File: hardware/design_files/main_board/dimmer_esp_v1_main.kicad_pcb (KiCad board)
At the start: 4 copper layers, 44 x 48.1 mm, 54 parts, among them IC1 PEC11S-929K-S0015, J1 Screw_Terminal_01x03, J2 SM05B-SRSS-TB_LF__SN_, J3 Conn_01x02, K1 FTR-LYCA005Y, Q1 BC817, SW1 Commission, SW2 Toggle, SW3 Reset, U1 SGM2212-3.3XKC3G/TR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

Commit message: Hardware: Switch button pin from GPIO09 (strapping pin) to GPIO23
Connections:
- R9 pad 2: /D09 -> /D23_commission
- SW1 pad 2: /D09 -> /D23_commission
- U4 pad 29: unconnected-(U4-IO23-Pad29) -> /D23_commission
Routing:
- net /D09: track 70.5 -> 0.00 mm, vias 3 -> 0
- net /D23_commission: track 0.00 -> 65.1 mm, vias 0 -> 4
- net GND: track 261.9 -> 263.3 mm
- net /D14: track 39.0 -> 38.4 mm

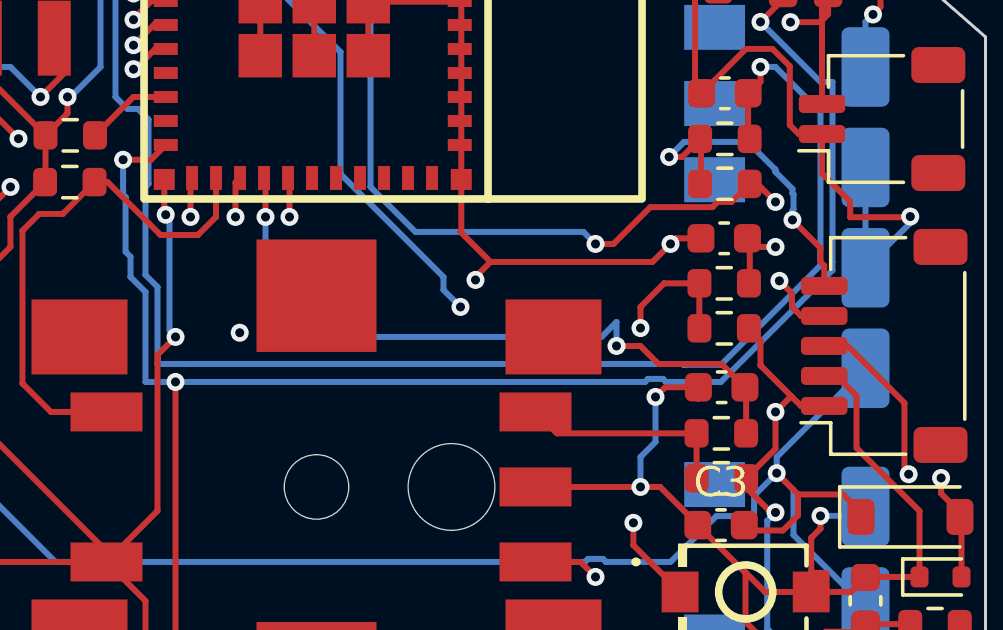
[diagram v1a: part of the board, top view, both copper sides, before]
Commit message: Hardware: Rename C9 back to C8, fix tracks
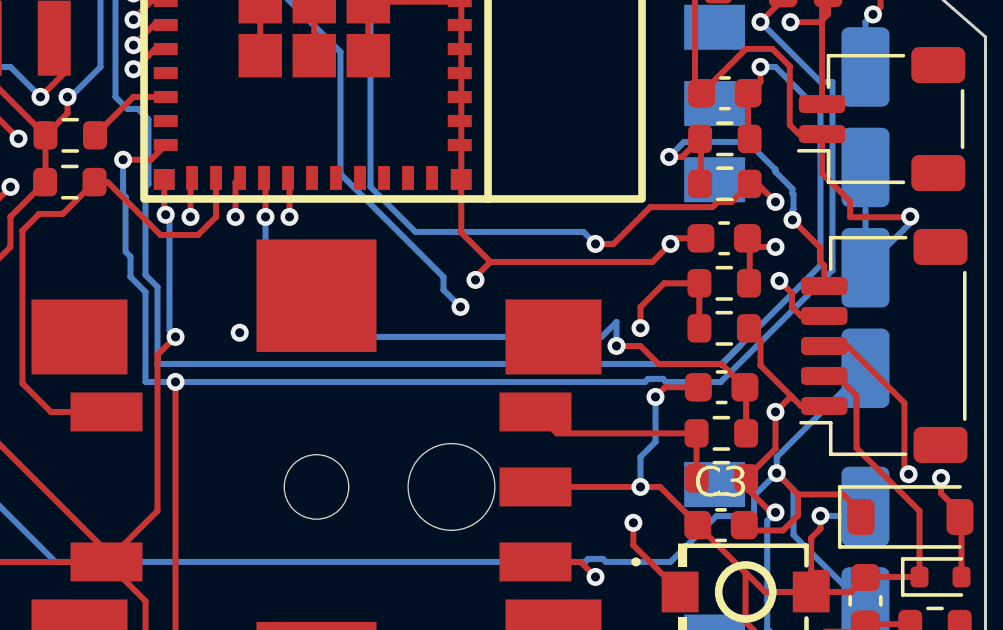
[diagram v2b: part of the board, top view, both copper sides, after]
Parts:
- renumbered C9 to C8
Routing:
- net /D06: track 50.3 -> 51.1 mm

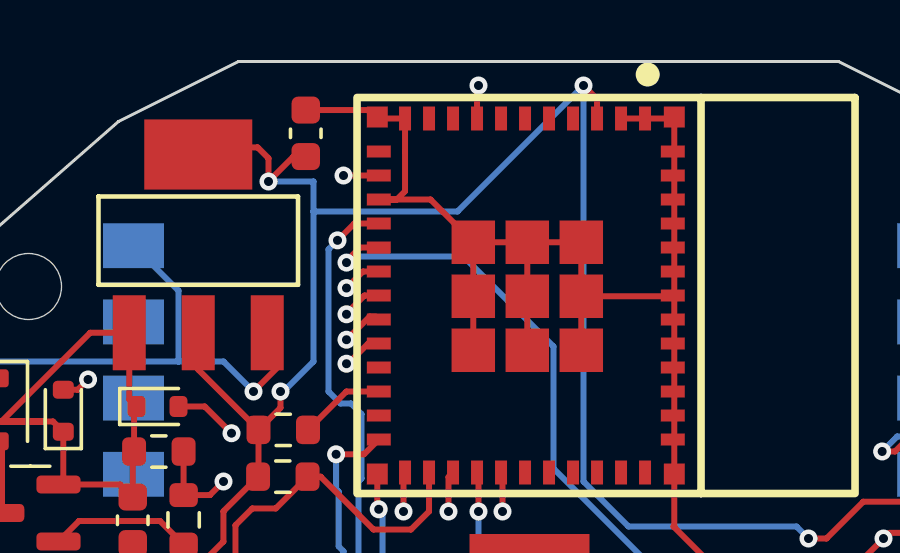
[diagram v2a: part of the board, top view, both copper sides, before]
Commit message: Hardware: Switch relay pin from D15 (strapping pin) to D02
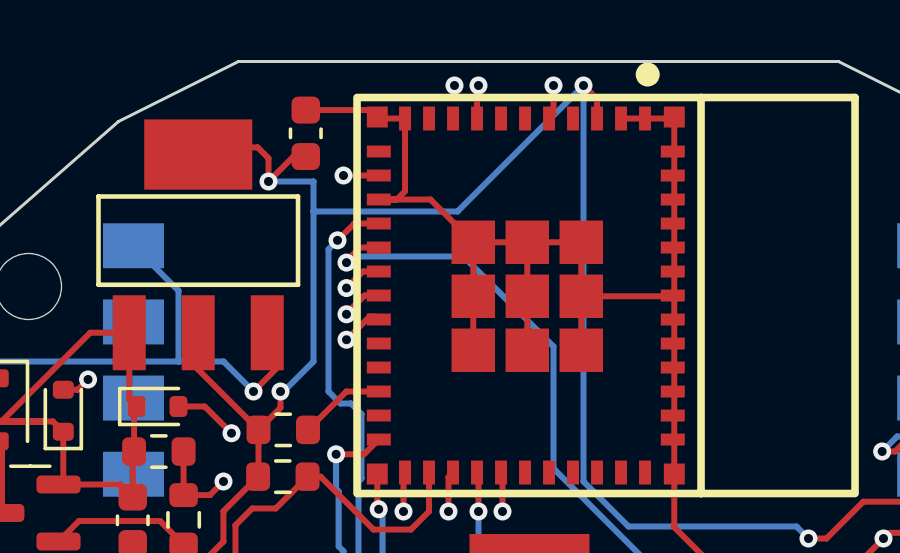
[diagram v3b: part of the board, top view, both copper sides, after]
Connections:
- R6 pad 2: /D15 -> /D02_relay
- R7 pad 2: /D15 -> /D02_relay
- U4 pad 20: /D15 -> unconnected-(U4-IO15-Pad20)
- U4 pad 5: unconnected-(U4-IO2-Pad5) -> /D02_relay
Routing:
- net /D02_relay: track 0.00 -> 24.5 mm, vias 0 -> 3
- net /D15: track 10.1 -> 0.00 mm, vias 2 -> 0
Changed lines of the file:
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@@
 			(layers "F.Cu" "F.Mask" "F.Paste")
 			(roundrect_rratio 0.25)
-			(net "/D15")
+			(net "/D02_relay")
 			(pintype "passive")
 		)
@@
 			(layers "F.Cu" "F.Mask" "F.Paste")
 			(roundrect_rratio 0.25)
-			(net "/D15")
+			(net "/D02_relay")
 			(pintype "passive")
 		)
@@
 			(size 0.8 0.4)
 			(layers "F.Cu" "F.Mask" "F.Paste")
-			(net "unconnected-(U4-IO2-Pad5)")
+			(net "/D02_relay")
 			(pinfunction "IO2_5")
-			(pintype "unspecified+no_connect")
+			(pintype "unspecified")
 		)
 		(pad "6" smd rect
@@
 			(size 0.8 0.4)
 			(layers "F.Cu" "F.Mask" "F.Paste")
-			(net "/D15")
+			(net "unconnected-(U4-IO15-Pad20)")
 			(pinfunction "IO15_20")
-			(pintype "unspecified")
+			(pintype "unspecified+no_connect")
 		)
 		(pad "21" smd rect
@@
 	)
 	(segment
-		(start 161.14994 47.074469)
-		(end 161.1 47.074469)
-		(width 0.2)
-		(layer "F.Cu")
-		(net "/D15")
-	)
-	(segment
-		(start 155.670433 50.001604)
-		(end 155.669923 50.001094)
-		(width 0.2)
-		(layer "F.Cu")
-		(net "/D15")
-	)
-	(segment
-		(start 156.546623 51.453377)
-		(end 157 51)
-		(width 0.2)
-		(layer "F.Cu")
-		(net "/D15")
-	)
-	(segment
-		(start 155.670433 51.453377)
-		(end 156.546623 51.453377)
-		(width 0.2)
-		(layer "F.Cu")
-		(net "/D15")
-	)
-	(segment
-		(start 161.823981 46.400428)
-		(end 161.14994 47.074469)
-		(width 0.2)
-		(layer "F.Cu")
-		(net "/D15")
-	)
-	(segment
-		(start 155.670433 51.453377)
-		(end 155.670433 50.001604)
-		(width 0.2)
-		(layer "F.Cu")
-		(net "/D15")
-	)
-	(segment
-		(start 162.176038 46.400428)
-		(end 161.823981 46.400428)
-		(width 0.2)
-		(layer "F.Cu")
-		(net "/D15")
-	)
-	(via
-		(at 157 51)
-		(size 0.6)
-		(drill 0.3)
-		(layers "F.Cu" "B.Cu")
-		(capping no)
-		(covering
-			(front no)
-			(back no)
-		)
-		(plugging
-			(front no)
-			(back no)
-		)
-		(filling no)
-		(net "/D15")
-	)
-	(via
-		(at 161.1 47.074469)
-		(size 0.6)
-		(drill 0.3)
-		(layers "F.Cu" "B.Cu")
-		(capping no)
-		(covering
-			(front no)
-			(back no)
-		)
-		(plugging
-			(front no)
-			(back no)
-		)
-		(filling no)
-		(net "/D15")
-	)
-	(segment
-		(start 160.925531 47.074469)
-		(end 157 51)
-		(width 0.2)
-		(layer "In2.Cu")
-		(net "/D15")
-	)
-	(segment
-		(start 161.1 47.074469)
-		(end 160.925531 47.074469)
-		(width 0.2)
-		(layer "In2.Cu")
-		(net "/D15")
-	)
-	(segment
 		(start 178.578602 79.000857)
 		(end 178.578602 79.427545)
@@
 		(net "/HV1")
 	)
+	(segment
+		(start 168 37.8)
+		(end 168 38.751466)
+		(width 0.2)
+		(layer "F.Cu")
+		(net "/D02_relay")
+	)
+	(segment
+		(start 155.670433 50.001604)
+		(end 155.669923 50.001094)
+		(width 0.2)
+		(layer "F.Cu")
+		(net "/D02_relay")
+	)
+	(segment
+		(start 156.546623 51.453377)
+		(end 157 51)
+		(width 0.2)
+		(layer "F.Cu")
+		(net "/D02_relay")
+	)
+	(segment
+		(start 155.670433 51.453377)
+		(end 156.546623 51.453377)
+		(width 0.2)
+		(layer "F.Cu")
+		(net "/D02_relay")
+	)
+	(segment
+		(start 168 38.751466)
+		(end 167.851038 38.900428)
+		(width 0.2)
+		(layer "F.Cu")
+		(net "/D02_relay")
+	)
+	(segment
+		(start 155.670433 51.453377)
+		(end 155.670433 50.001604)
+		(width 0.2)
+		(layer "F.Cu")
+		(net "/D02_relay")
+	)
+	(via
+		(at 168 37.8)
+		(size 0.6)
+		(drill 0.3)
+		(layers "F.Cu" "B.Cu")
+		(net "/D02_relay")
+	)
+	(via
+		(at 157 51)
+		(size 0.6)
+		(drill 0.3)
+		(layers "F.Cu" "B.Cu")
+		(capping no)
+		(covering
+			(front no)
+			(back no)
+		)
+		(plugging
+			(front no)
+			(back no)
+		)
+		(filling no)
+		(net "/D02_relay")
+	)
+	(via
+		(at 164.699998 37.799999)
+		(size 0.6)
+		(drill 0.3)
+		(layers "F.Cu" "B.Cu")
+		(net "/D02_relay")
+	)
+	(segment
+		(start 164.699998 37.848527)
+		(end 165.251471 38.4)
+		(width 0.2)
+		(layer "In1.Cu")
+		(net "/D02_relay")
+	)
+	(segment
+		(start 164.699998 37.799999)
+		(end 164.699998 37.848527)
+		(width 0.2)
+		(layer "In1.Cu")
+		(net "/D02_relay")
+	)
+	(segment
+		(start 167.4 38.4)
+		(end 168 37.8)
+		(width 0.2)
+		(layer "In1.Cu")
+		(net "/D02_relay")
+	)
+	(segment
+		(start 165.251471 38.4)
+		(end 167.4 38.4)
+		(width 0.2)
+		(layer "In1.Cu")
+		(net "/D02_relay")
+	)
+	(segment
+		(start 160.925531 47.074469)
+		(end 161.148526 47.074469)
+		(width 0.2)
+		(layer "In2.Cu")
+		(net "/D02_relay")
+	)
+	(segment
+		(start 161.148526 47.074469)
+		(end 164.699998 43.522997)
+		(width 0.2)
+		(layer "In2.Cu")
+		(net "/D02_relay")
+	)
+	(segment
+		(start 164.699998 43.522997)
+		(end 164.699998 37.799999)
+		(width 0.2)
+		(layer "In2.Cu")
+		(net "/D02_relay")
+	)
+	(segment
+		(start 157 51)
+		(end 160.925531 47.074469)
+		(width 0.2)
+		(layer "In2.Cu")
+		(net "/D02_relay")
+	)
 	(group ""
